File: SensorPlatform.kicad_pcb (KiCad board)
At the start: 2 copper layers, 70.5 x 88.9 mm, 37 parts, among them J1 Conn_01x19, J2 Conn_01x19, Q1 Q_NPN_BCE, Q2 Q_NPN_BCE, SW1 SW_Push, SW2 SW_Push, U1 AMS1117-3.3, U2 USB_CON8, U3 CP2102N, U4 ESP32-WROOM-32

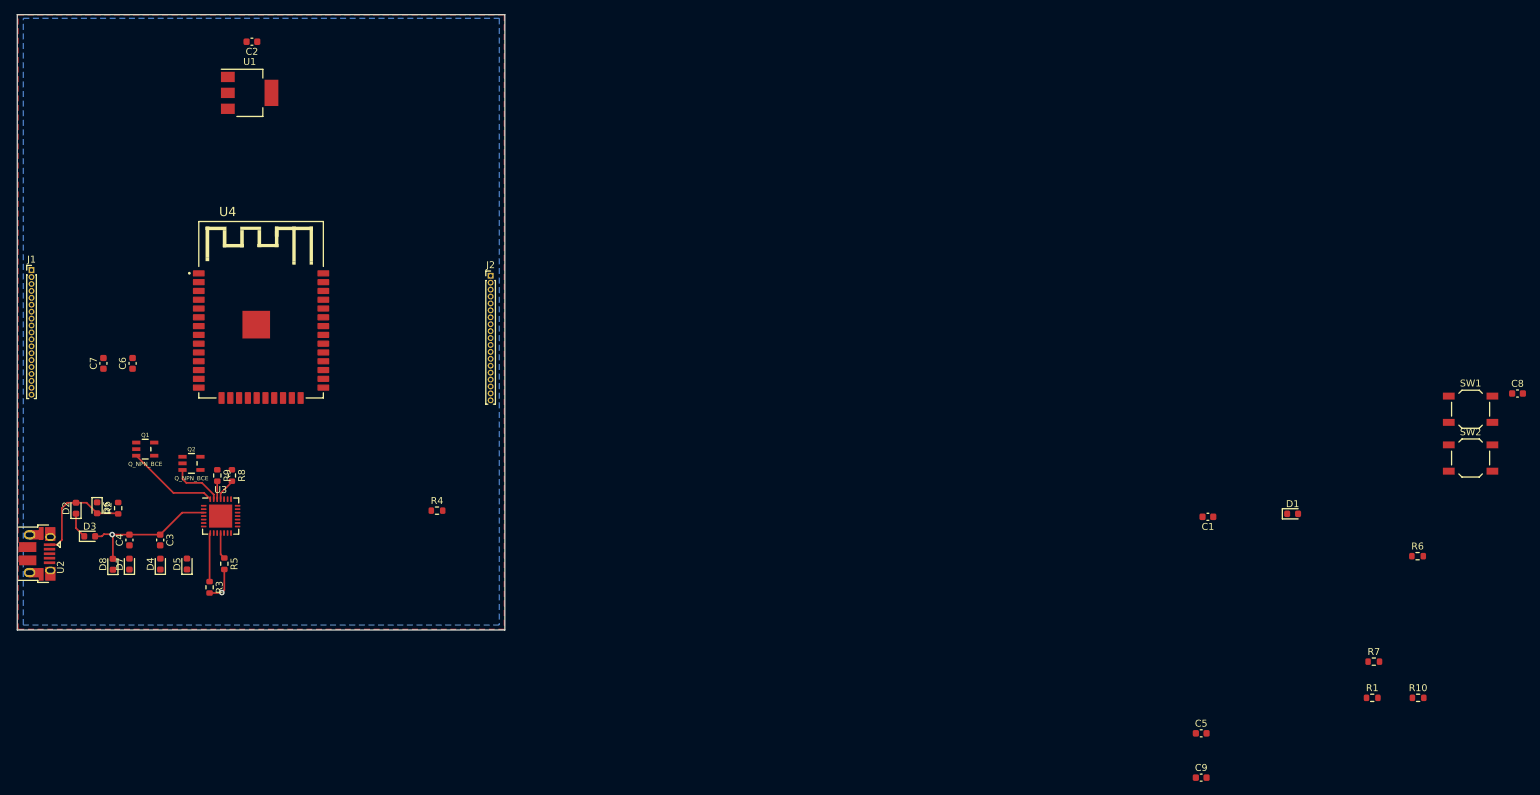
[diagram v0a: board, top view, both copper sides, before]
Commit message: Routed most PCB traces
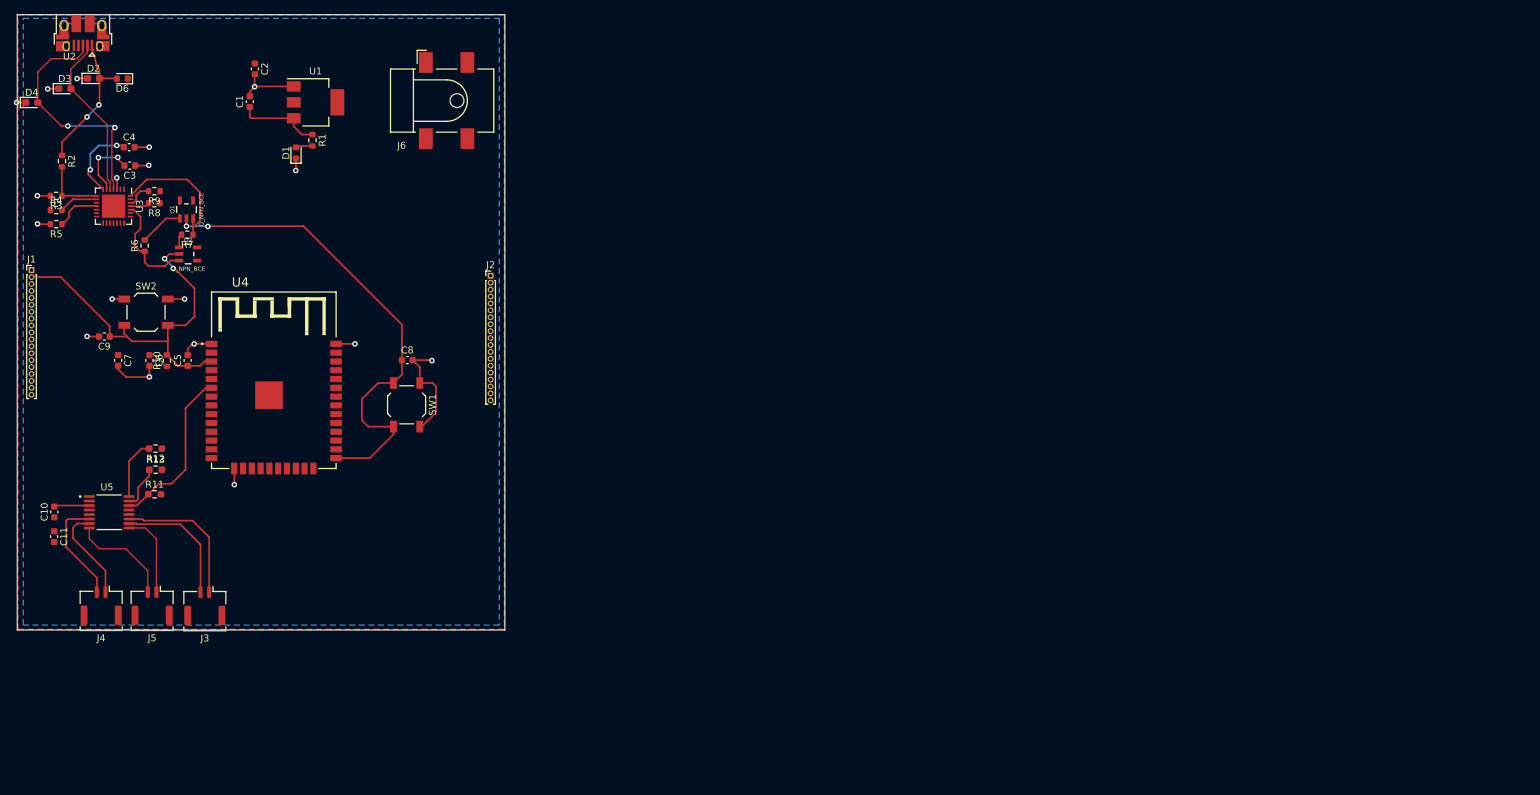
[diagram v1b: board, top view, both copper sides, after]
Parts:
- removed D5, D7, D8: D_Zener_Small_ALT, Diode_SMD:D_0603_1608Metric
- added C10: 0.1u, Capacitor_SMD:C_0603_1608Metric, F.Cu at (39.5, 108.5)
- added C11: 0.1u, Capacitor_SMD:C_0603_1608Metric, F.Cu at (39.5, 112.1)
- added J3: Conn_01x02, Connector_Molex:Molex_CLIK-Mate_502382-0270_1x02-1MP_P1.25mm_Vertical, F.Cu at (61.3, 122.0)
- added J4: Conn_01x02, Connector_Molex:Molex_CLIK-Mate_502382-0270_1x02-1MP_P1.25mm_Vertical, F.Cu at (46.3, 122.0)
- added J5: Conn_01x02, Connector_Molex:Molex_CLIK-Mate_502382-0270_1x02-1MP_P1.25mm_Vertical, F.Cu at (53.7, 122.0)
- added J6: Barrel_Jack, Connector_BarrelJack:BarrelJack_CLIFF_FC681465S_SMT_Horizontal, F.Cu at (96.2, 49.0)
- added R11: R, Resistor_SMD:R_0603_1608Metric_Pad0.98x0.95mm_HandSolder, F.Cu at (54.0, 105.9)
- added R12: R, Resistor_SMD:R_0603_1608Metric_Pad0.98x0.95mm_HandSolder, F.Cu at (54.2, 99.3)
- added R13: R, Resistor_SMD:R_0603_1608Metric_Pad0.98x0.95mm_HandSolder, F.Cu at (54.2, 102.4)
- added U5: ADS122C04IPWR, ADC:SOP65P640X120-16N, F.Cu at (47.5, 108.5)
- D2, D3, D4: value D_Zener_Small_ALT -> 1.5KExxCA; footprint Diode_SMD:D_0603_1608Metric -> Diode_SMD:D_0603_1608Metric_Pad1.05x0.95mm_HandSolder
- moved SW2 192.6 mm to (52.8, 79.6)
- moved R6 189.3 mm to (52.6, 70.0), turned to 90 degrees
- moved R10 187.3 mm to (55.8, 86.6), turned to 90 degrees
- moved R7 182.2 mm to (58.8, 68.4), turned to 180 degrees
- moved R1 173.1 mm to (76.8, 54.8), turned to -90 degrees
- moved C9 170.8 mm to (46.8, 83.1), turned to 180 degrees
- moved C8 160.5 mm to (90.5, 86.5)
- moved C5 156.1 mm to (58.8, 86.6), turned to 90 degrees
- moved SW1 153.8 mm to (90.5, 93.0), turned to -90 degrees
- moved D1 153.2 mm to (74.5, 56.6), turned to 90 degrees
- moved C1 150.9 mm to (67.8, 49.2), turned to 90 degrees
- moved U2 75.5 mm to (43.7, 39.3), turned to 180 degrees
- moved R4 70.1 mm to (39.8, 64.9)
- moved D4 69.2 mm to (36.3, 49.3), turned to 0 degrees
- moved D3 64.8 mm to (41.1, 47.3)
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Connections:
- D2 pad 1: Net-(D2-Pad1) -> GND
- D3 pad 1: Net-(D2-Pad1) -> GND
- D3 pad 2: GND -> USB_DN
- D4 pad 1: Net-(D4-Pad1) -> GND
- D4 pad 2: USB_DN -> USB_DP
- Q1 pad 2: /Micro USB 5v and USB-UART/IO0 -> IO0
- Q2 pad 2: /Micro USB 5v and USB-UART/EN -> EN
- Q2 pad 3: DSR -> RTS
- R6 pad 1: DSR -> RTS
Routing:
- net IO0: track 0.00 -> 71.5 mm, vias 0 -> 2
- net EN: track 0.00 -> 54.9 mm, vias 0 -> 2
- net GND: track 26.0 -> 71.0 mm, vias 2 -> 18
- net USB_DP: track 0.00 -> 35.0 mm, vias 0 -> 2
- net +3V3: track 0.00 -> 26.2 mm, vias 0 -> 4
- net IO34: track 0.00 -> 24.2 mm
- net USB_DN: track 0.00 -> 24.1 mm
- net AIN0: track 0.00 -> 20.6 mm
- net AIN1: track 0.00 -> 18.5 mm
- net AIN3: track 0.00 -> 15.6 mm
- net RTS: track 0.00 -> 15.3 mm
- net REFN: track 0.00 -> 15.0 mm
- net AIN2: track 0.00 -> 13.8 mm
- net REFP: track 0.00 -> 12.3 mm
- net Net-(C1-Pad1): track 0.00 -> 12.2 mm
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
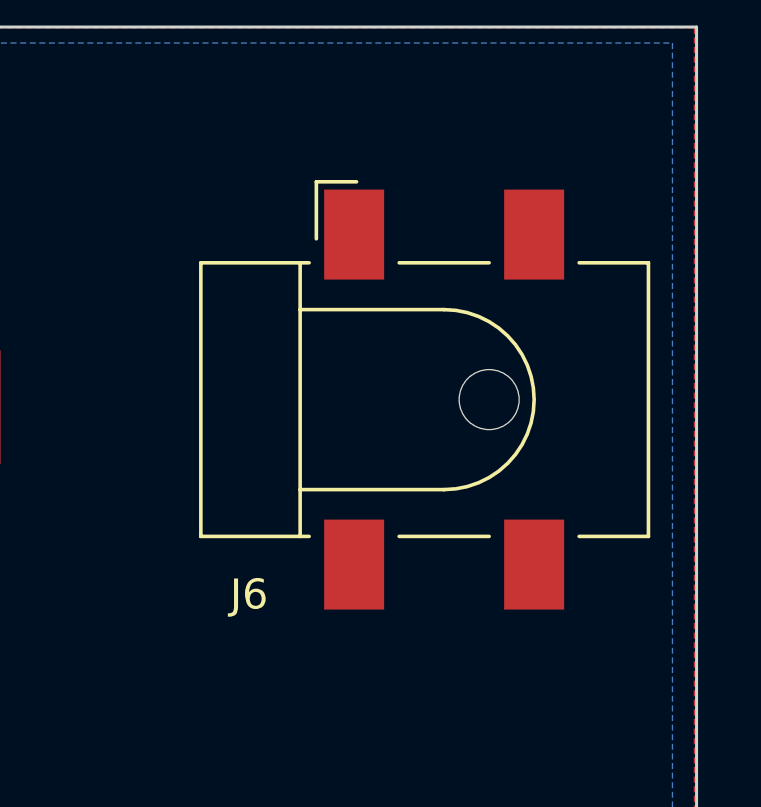
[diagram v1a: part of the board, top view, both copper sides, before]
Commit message: Added VOC and Optical Sensors
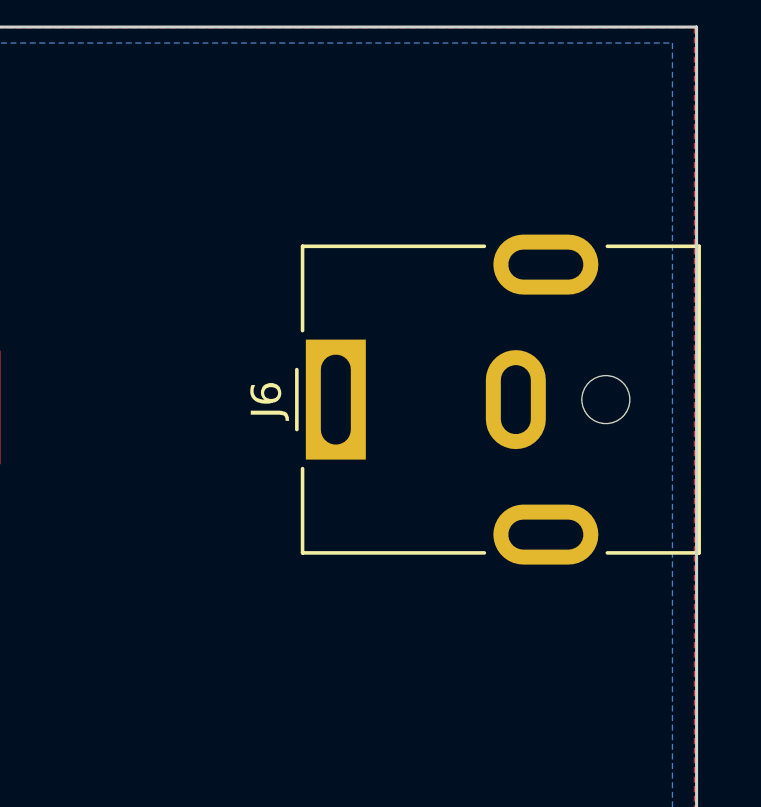
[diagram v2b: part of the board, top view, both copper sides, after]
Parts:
- J6: footprint Connector_BarrelJack:BarrelJack_CLIFF_FC681465S_SMT_Horizontal -> Connector_BarrelJack:BarrelJack_CUI_PJ-063AH_Horizontal
- moved J6 3.61 mm to (92.6, 49.0), turned to 90 degrees
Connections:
- C1 pad 1: Net-(C1-Pad1) -> +5V
- R1 pad 1: Net-(C1-Pad1) -> +5V
- U1 pad 3: Net-(C1-Pad1) -> +5V
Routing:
- net Net-(C1-Pad1): track 12.2 -> 0.00 mm
- net +5V: track 0.00 -> 12.2 mm

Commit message: Vertical Horizontal Traces
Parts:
- removed the C1 at (67.8, 49.2)
- removed the C10 at (39.5, 108.5)
- removed the C11 at (39.5, 112.1)
- removed the C2 at (68.5, 44.5)
- removed the C3 at (50.5, 58.4)
- removed the C4 at (50.4, 55.8)
- removed the C5 at (58.8, 86.6)
- removed the C6 at (53.3, 86.6)
- removed the C7 at (48.8, 86.6)
- removed the C8 at (90.5, 86.5)
- removed the C9 at (46.8, 83.1)
- removed the D1 at (74.5, 56.6)
- removed the D2 at (45.2, 45.8)
- removed the D3 at (41.1, 47.3)
- removed the D4 at (36.3, 49.3)
- removed the D6 at (49.4, 45.9)
- removed the J1 at (36.2, 73.5)
- removed the J2 at (102.6, 74.4)
- removed the J3 at (61.3, 122.0)
- removed the J4 at (46.3, 122.0)
- removed the J5 at (53.7, 122.0)
- removed the J6 at (92.6, 49.0)
- removed the Q1 at (58.6, 64.8)
- removed the Q2 at (58.9, 71.2)
- removed the R1 at (76.8, 54.8)
- removed the R10 at (55.8, 86.6)
- removed the R11 at (54.0, 105.9)
- removed the R12 at (54.2, 99.3)
- removed the R13 at (54.2, 102.4)
- removed the R2 at (40.6, 57.8)
- removed the R3 at (39.8, 62.8)
- removed the R4 at (39.8, 64.9)
- removed the R5 at (39.8, 66.9)
- removed the R6 at (52.6, 70.0)
- removed the R7 at (58.8, 68.4)
- removed the R8 at (54.0, 63.9)
- removed the R9 at (54.0, 62.1)
- removed the SW1 at (90.5, 93.0)
- removed the SW2 at (52.8, 79.6)
- removed the U1 at (77.3, 49.3)
- removed U2: USB_CON8, Connector_USB:USB_Micro-B_Amphenol_10103594-0001LF_Horizontal
- removed the U3 at (48.1, 64.3)
- removed the U4 at (71.3, 92.5)
- removed the U5 at (47.5, 108.5)
- added C1: 22u, Capacitor_SMD:C_0603_1608Metric, F.Cu at (452.6, 116.3)
- added C1: 22u, Capacitor_SMD:C_0603_1608Metric, F.Cu at (157.5, 110.2)
- added C10: 0.1u, Capacitor_SMD:C_0603_1608Metric, F.Cu at (411.8, 137.8)
- added C10: 0.1u, Capacitor_SMD:C_0603_1608Metric, F.Cu at (116.8, 131.7)
- added C11: 0.1u, Capacitor_SMD:C_0603_1608Metric, F.Cu at (109.7, 139.4)
- added C11: 0.1u, Capacitor_SMD:C_0603_1608Metric, F.Cu at (404.7, 145.4)
- added C12: 0.1u, Capacitor_SMD:C_0603_1608Metric, F.Cu at (422.2, 119.4)
- added C12: 0.1u, Capacitor_SMD:C_0603_1608Metric, F.Cu at (127.2, 113.3)
- added C13: 10u, Capacitor_SMD:C_0603_1608Metric, F.Cu at (116.7, 125.0)
- added C13: 10u, Capacitor_SMD:C_0603_1608Metric, F.Cu at (411.7, 131.1)
- added C14: 0.1u, Capacitor_SMD:C_0603_1608Metric, F.Cu at (411.9, 134.2)
- added C14: 0.1u, Capacitor_SMD:C_0603_1608Metric, F.Cu at (116.9, 128.1)
- added C15: 10u, Capacitor_SMD:C_0603_1608Metric, F.Cu at (412.5, 99.4)
- added C15: 10u, Capacitor_SMD:C_0603_1608Metric, F.Cu at (117.5, 93.3)
- added C16: 10u, Capacitor_SMD:C_0603_1608Metric, F.Cu at (416.8, 117.5)
- added C16: 10u, Capacitor_SMD:C_0603_1608Metric, F.Cu at (121.8, 111.4)
- added C17: 0.1u, Capacitor_SMD:C_0603_1608Metric, F.Cu at (118.0, 109.7)
- added C17: 0.1u, Capacitor_SMD:C_0603_1608Metric, F.Cu at (413.0, 115.8)
- added C18: 1u, Capacitor_SMD:C_0603_1608Metric, F.Cu at (139.4, 103.6)
- added C18: 1u, Capacitor_SMD:C_0603_1608Metric, F.Cu at (434.4, 109.7)
- added C19: 0.1u, Capacitor_SMD:C_0603_1608Metric, F.Cu at (99.9, 146.6)
- added C19: 0.1u, Capacitor_SMD:C_0603_1608Metric, F.Cu at (395.0, 153.0)
- added C2: 22u, Capacitor_SMD:C_0603_1608Metric, F.Cu at (157.5, 113.5)
- added C2: 22u, Capacitor_SMD:C_0603_1608Metric, F.Cu at (452.6, 119.6)
- added C20: 0.1u, Capacitor_SMD:C_0603_1608Metric, F.Cu at (399.1, 157.7)
- added C20: 0.1u, Capacitor_SMD:C_0603_1608Metric, F.Cu at (104.1, 151.6)
- added C21: 0.1u, Capacitor_SMD:C_0603_1608Metric, F.Cu at (87.6, 133.5)
- added C21: 0.1u, Capacitor_SMD:C_0603_1608Metric, F.Cu at (382.6, 139.6)
- added C22: 0.1u, Capacitor_SMD:C_0603_1608Metric, F.Cu at (395.2, 147.2)
- added C22: 0.1u, Capacitor_SMD:C_0603_1608Metric, F.Cu at (100.2, 141.1)
- added C3: 4.7u, Capacitor_SMD:C_0603_1608Metric, F.Cu at (155.8, 131.8)
- added C3: 4.7u, Capacitor_SMD:C_0603_1608Metric, F.Cu at (450.8, 137.9)
- added C4: 0.1u, Capacitor_SMD:C_0603_1608Metric, F.Cu at (174.6, 133.1)
- added C4: 0.1u, Capacitor_SMD:C_0603_1608Metric, F.Cu at (469.6, 139.2)
- added C5: 0.1u, Capacitor_SMD:C_0603_1608Metric, F.Cu at (114.6, 38.6)
- added C5: 0.1u, Capacitor_SMD:C_0603_1608Metric, F.Cu at (409.6, 44.7)
- added C6: 22u, Capacitor_SMD:C_0603_1608Metric, F.Cu at (403.3, 48.5)
- added C6: 22u, Capacitor_SMD:C_0603_1608Metric, F.Cu at (108.3, 42.4)
- added C7: 0.1u, Capacitor_SMD:C_0603_1608Metric, F.Cu at (108.3, 38.6)
- added C7: 0.1u, Capacitor_SMD:C_0603_1608Metric, F.Cu at (403.3, 44.7)
- added C8: 0.1u, Capacitor_SMD:C_0603_1608Metric, F.Cu at (147.1, 53.1)
- added C8: 0.1u, Capacitor_SMD:C_0603_1608Metric, F.Cu at (442.1, 59.2)
- added C9: 0.1u, Capacitor_SMD:C_0603_1608Metric, F.Cu at (409.6, 48.5)
- added C9: 0.1u, Capacitor_SMD:C_0603_1608Metric, F.Cu at (114.6, 42.4)
- added D1: LED, LED_SMD:LED_0603_1608Metric, F.Cu at (452.6, 122.7)
- added D1: LED, LED_SMD:LED_0603_1608Metric, F.Cu at (157.5, 116.6)
- added D10: D_TVS, Diode_SMD:D_0402_1005Metric_Pad0.77x0.64mm_HandSolder, F.Cu at (174.6, 127.8)
- added D10: D_TVS, Diode_SMD:D_0402_1005Metric_Pad0.77x0.64mm_HandSolder, F.Cu at (469.6, 133.8)
- added D11: D_TVS, Diode_SMD:D_0402_1005Metric_Pad0.77x0.64mm_HandSolder, F.Cu at (112.7, 110.4)
- added D11: D_TVS, Diode_SMD:D_0402_1005Metric_Pad0.77x0.64mm_HandSolder, F.Cu at (407.7, 116.5)
- added D12: D_TVS, Diode_SMD:D_0402_1005Metric_Pad0.77x0.64mm_HandSolder, F.Cu at (121.5, 120.9)
- added D12: D_TVS, Diode_SMD:D_0402_1005Metric_Pad0.77x0.64mm_HandSolder, F.Cu at (416.5, 127.0)
- added D13: D_Zener_Small_ALT, Diode_SMD:D_0603_1608Metric, F.Cu at (159.1, 104.9)
- added D13: D_Zener_Small_ALT, Diode_SMD:D_0603_1608Metric, F.Cu at (454.1, 111.0)
- added D2: 1.5KExxCA, Diode_SMD:D_0603_1608Metric_Pad1.05x0.95mm_HandSolder, F.Cu at (463.0, 144.8)
- added D2: 1.5KExxCA, Diode_SMD:D_0603_1608Metric_Pad1.05x0.95mm_HandSolder, F.Cu at (168.0, 138.7)
- added D3: 1.5KExxCA, Diode_SMD:D_0603_1608Metric_Pad1.05x0.95mm_HandSolder, F.Cu at (459.7, 149.2)
- added D3: 1.5KExxCA, Diode_SMD:D_0603_1608Metric_Pad1.05x0.95mm_HandSolder, F.Cu at (164.7, 143.1)
- added D4: 1.5KExxCA, Diode_SMD:D_0603_1608Metric_Pad1.05x0.95mm_HandSolder, F.Cu at (163.9, 138.7)
- added D4: 1.5KExxCA, Diode_SMD:D_0603_1608Metric_Pad1.05x0.95mm_HandSolder, F.Cu at (458.9, 144.8)
- added D5: LED, LED_SMD:LED_0603_1608Metric_Pad1.05x0.95mm_HandSolder, F.Cu at (109.3, 112.4)
- added D5: LED, LED_SMD:LED_0603_1608Metric_Pad1.05x0.95mm_HandSolder, F.Cu at (404.3, 118.5)
- added D6: D_Zener_Small_ALT, Diode_SMD:D_0603_1608Metric, F.Cu at (453.3, 155.7)
- added D6: D_Zener_Small_ALT, Diode_SMD:D_0603_1608Metric, F.Cu at (158.3, 149.6)
- added D7: LED, LED_SMD:LED_0603_1608Metric_Pad1.05x0.95mm_HandSolder, F.Cu at (110.9, 90.4)
- added D7: LED, LED_SMD:LED_0603_1608Metric_Pad1.05x0.95mm_HandSolder, F.Cu at (405.9, 96.5)
- added D8: LED, LED_SMD:LED_0603_1608Metric_Pad1.05x0.95mm_HandSolder, F.Cu at (416.5, 102.7)
- added D8: LED, LED_SMD:LED_0603_1608Metric_Pad1.05x0.95mm_HandSolder, F.Cu at (121.5, 97.6)
- added D9: LED, LED_SMD:LED_0603_1608Metric_Pad1.05x0.95mm_HandSolder, F.Cu at (126.2, 118.0)
- added D9: LED, LED_SMD:LED_0603_1608Metric_Pad1.05x0.95mm_HandSolder, F.Cu at (421.2, 124.1)
- added J1: Conn_01x19, Connector_PinHeader_2.54mm:PinHeader_1x19_P2.54mm_Vertical, F.Cu at (93.2, 47.5)
- added J1: Conn_01x19, Connector_PinHeader_2.54mm:PinHeader_1x19_P2.54mm_Vertical, F.Cu at (388.2, 53.6)
- added J10: 110990030, Seeed:SEEED_110990030, F.Cu at (162.5, 56.0)
- added J10: 110990030, Seeed:SEEED_110990030, F.Cu at (457.5, 62.1)
- added J2: Conn_01x19, Connector_PinHeader_2.54mm:PinHeader_1x19_P2.54mm_Vertical, F.Cu at (464.7, 53.6)
- added J2: Conn_01x19, Connector_PinHeader_2.54mm:PinHeader_1x19_P2.54mm_Vertical, F.Cu at (169.7, 47.5)
- added J3: Conn_01x02, Connector_PinHeader_2.54mm:PinHeader_1x02_P2.54mm_Vertical, F.Cu at (105.8, 142.7)
- added J3: Conn_01x02, Connector_PinHeader_2.54mm:PinHeader_1x02_P2.54mm_Vertical, F.Cu at (400.8, 148.8)
- added J4: Conn_01x02, Connector_PinHeader_2.54mm:PinHeader_1x02_P2.54mm_Vertical, F.Cu at (110.9, 142.9)
- added J4: Conn_01x02, Connector_PinHeader_2.54mm:PinHeader_1x02_P2.54mm_Vertical, F.Cu at (405.9, 149.0)
- added J5: Conn_01x02, Connector_PinHeader_2.54mm:PinHeader_1x02_P2.54mm_Vertical, F.Cu at (413.6, 148.4)
- added J5: Conn_01x02, Connector_PinHeader_2.54mm:PinHeader_1x02_P2.54mm_Vertical, F.Cu at (118.6, 142.3)
- added J6: Barrel_Jack, Connector_BarrelJack:BarrelJack_CUI_PJ-063AH_Horizontal, F.Cu at (459.3, 110.7)
- added J6: Barrel_Jack, Connector_BarrelJack:BarrelJack_CUI_PJ-063AH_Horizontal, F.Cu at (164.2, 104.6)
- added J7: Conn_01x04, Connector_PinHeader_2.54mm:PinHeader_1x04_P2.54mm_Vertical, F.Cu at (110.0, 54.9)
- added J7: Conn_01x04, Connector_PinHeader_2.54mm:PinHeader_1x04_P2.54mm_Vertical, F.Cu at (405.1, 61.0)
- added J8: Conn_01x08, Connector_PinHeader_2.54mm:PinHeader_1x08_P2.54mm_Vertical, F.Cu at (93.2, 100.0)
- added J8: Conn_01x08, Connector_PinHeader_2.54mm:PinHeader_1x08_P2.54mm_Vertical, F.Cu at (388.2, 106.1)
- added J9: QWIIC_CONNECTORSR, SparkfunConnectors:1X04_1MM_RA_STRESSRELIEF, F.Cu at (157.3, 67.6)
- added J9: QWIIC_CONNECTORSR, SparkfunConnectors:1X04_1MM_RA_STRESSRELIEF, F.Cu at (452.3, 73.6)
- added JP1: Jumper, Jumper:SolderJumper-2_P1.3mm_Bridged_RoundedPad1.0x1.5mm, F.Cu at (97.4, 118.3)
- added JP1: Jumper, Jumper:SolderJumper-2_P1.3mm_Bridged_RoundedPad1.0x1.5mm, F.Cu at (392.4, 124.4)
- added Q1: Q_NPN_BCE, Package_TO_SOT_SMD:SOT-23, F.Cu at (443.2, 141.2)
- added Q1: Q_NPN_BCE, Package_TO_SOT_SMD:SOT-23, F.Cu at (148.2, 135.1)
- added Q2: Q_NPN_BCE, Package_TO_SOT_SMD:SOT-23, F.Cu at (454.6, 134.3)
- added Q2: Q_NPN_BCE, Package_TO_SOT_SMD:SOT-23, F.Cu at (159.6, 128.3)
- added R1: 2k, Resistor_SMD:R_0603_1608Metric_Pad0.98x0.95mm_HandSolder, F.Cu at (153.5, 116.6)
- added R1: 2k, Resistor_SMD:R_0603_1608Metric_Pad0.98x0.95mm_HandSolder, F.Cu at (448.5, 122.7)
- added R10: 10k, Resistor_SMD:R_0603_1608Metric_Pad0.98x0.95mm_HandSolder, F.Cu at (395.9, 44.7)
- added R10: 10k, Resistor_SMD:R_0603_1608Metric_Pad0.98x0.95mm_HandSolder, F.Cu at (100.9, 38.6)
- added R11: R, Resistor_SMD:R_0603_1608Metric_Pad0.98x0.95mm_HandSolder, F.Cu at (395.3, 144.2)
- added R11: R, Resistor_SMD:R_0603_1608Metric_Pad0.98x0.95mm_HandSolder, F.Cu at (100.4, 139.4)
- added R12: R, Resistor_SMD:R_0603_1608Metric_Pad0.98x0.95mm_HandSolder, F.Cu at (90.5, 135.1)
- added R12: R, Resistor_SMD:R_0603_1608Metric_Pad0.98x0.95mm_HandSolder, F.Cu at (385.5, 141.2)
- added R13: R, Resistor_SMD:R_0603_1608Metric_Pad0.98x0.95mm_HandSolder, F.Cu at (395.1, 140.8)
- added R13: R, Resistor_SMD:R_0603_1608Metric_Pad0.98x0.95mm_HandSolder, F.Cu at (100.0, 134.7)
- added R14: R, Resistor_SMD:R_0603_1608Metric_Pad0.98x0.95mm_HandSolder, F.Cu at (389.2, 137.8)
- added R14: R, Resistor_SMD:R_0603_1608Metric_Pad0.98x0.95mm_HandSolder, F.Cu at (93.6, 131.8)
- added R15: R, Resistor_SMD:R_0603_1608Metric_Pad0.98x0.95mm_HandSolder, F.Cu at (385.9, 137.8)
- added R15: R, Resistor_SMD:R_0603_1608Metric_Pad0.98x0.95mm_HandSolder, F.Cu at (90.0, 131.8)
- added R16: 10k, Resistor_SMD:R_0603_1608Metric_Pad0.98x0.95mm_HandSolder, F.Cu at (105.3, 107.7)
- added R16: 10k, Resistor_SMD:R_0603_1608Metric_Pad0.98x0.95mm_HandSolder, F.Cu at (400.3, 113.8)
- added R17: 2.2k, Resistor_SMD:R_0603_1608Metric_Pad0.98x0.95mm_HandSolder, F.Cu at (121.4, 100.8)
- added R17: 2.2k, Resistor_SMD:R_0603_1608Metric_Pad0.98x0.95mm_HandSolder, F.Cu at (416.4, 106.9)
- added R18: 10k, Resistor_SMD:R_0603_1608Metric_Pad0.98x0.95mm_HandSolder, F.Cu at (99.5, 102.1)
- added R18: 10k, Resistor_SMD:R_0603_1608Metric_Pad0.98x0.95mm_HandSolder, F.Cu at (394.5, 108.2)
- added R19: 2.2k, Resistor_SMD:R_0603_1608Metric_Pad0.98x0.95mm_HandSolder, F.Cu at (120.2, 104.8)
- added R19: 2.2k, Resistor_SMD:R_0603_1608Metric_Pad0.98x0.95mm_HandSolder, F.Cu at (415.2, 110.9)
- added R2: 22.1k, Resistor_SMD:R_0603_1608Metric_Pad0.98x0.95mm_HandSolder, F.Cu at (453.3, 151.9)
- added R2: 22.1k, Resistor_SMD:R_0603_1608Metric_Pad0.98x0.95mm_HandSolder, F.Cu at (158.3, 145.8)
- added R20: 0, Resistor_SMD:R_0603_1608Metric_Pad0.98x0.95mm_HandSolder, F.Cu at (115.0, 100.9)
- added R20: 0, Resistor_SMD:R_0603_1608Metric_Pad0.98x0.95mm_HandSolder, F.Cu at (410.0, 107.0)
- added R21: 0, Resistor_SMD:R_0603_1608Metric_Pad0.98x0.95mm_HandSolder, F.Cu at (111.2, 103.6)
- added R21: 0, Resistor_SMD:R_0603_1608Metric_Pad0.98x0.95mm_HandSolder, F.Cu at (408.1, 110.1)
- added R22: 10k, Resistor_SMD:R_0603_1608Metric_Pad0.98x0.95mm_HandSolder, F.Cu at (396.2, 102.1)
- added R22: 10k, Resistor_SMD:R_0603_1608Metric_Pad0.98x0.95mm_HandSolder, F.Cu at (101.2, 96.1)
- added R23: 10k, Resistor_SMD:R_0603_1608Metric_Pad0.98x0.95mm_HandSolder, F.Cu at (106.6, 93.9)
- added R23: 10k, Resistor_SMD:R_0603_1608Metric_Pad0.98x0.95mm_HandSolder, F.Cu at (401.6, 100.0)
- added R24: 200, Resistor_SMD:R_0603_1608Metric_Pad0.98x0.95mm_HandSolder, F.Cu at (108.3, 108.2)
- added R24: 200, Resistor_SMD:R_0603_1608Metric_Pad0.98x0.95mm_HandSolder, F.Cu at (403.3, 114.3)
- added R25: 200, Resistor_SMD:R_0603_1608Metric_Pad0.98x0.95mm_HandSolder, F.Cu at (410.1, 102.6)
- added R25: 200, Resistor_SMD:R_0603_1608Metric_Pad0.98x0.95mm_HandSolder, F.Cu at (115.0, 97.6)
- added R26: R, Resistor_SMD:R_0603_1608Metric_Pad0.98x0.95mm_HandSolder, F.Cu at (126.1, 87.8)
- added R26: R, Resistor_SMD:R_0603_1608Metric_Pad0.98x0.95mm_HandSolder, F.Cu at (418.6, 93.9)
- added R27: 200, Resistor_SMD:R_0603_1608Metric_Pad0.98x0.95mm_HandSolder, F.Cu at (131.4, 118.1)
- added R27: 200, Resistor_SMD:R_0603_1608Metric_Pad0.98x0.95mm_HandSolder, F.Cu at (426.4, 124.2)
- added R28: R, Resistor_SMD:R_0603_1608Metric_Pad0.98x0.95mm_HandSolder, F.Cu at (98.2, 128.0)
- added R28: R, Resistor_SMD:R_0603_1608Metric_Pad0.98x0.95mm_HandSolder, F.Cu at (393.3, 134.1)
- added R29: R, Resistor_SMD:R_0603_1608Metric_Pad0.98x0.95mm_HandSolder, F.Cu at (403.1, 92.9)
- added R29: R, Resistor_SMD:R_0603_1608Metric_Pad0.98x0.95mm_HandSolder, F.Cu at (108.1, 86.9)
- added R3: 47.5k, Resistor_SMD:R_0603_1608Metric_Pad0.98x0.95mm_HandSolder, F.Cu at (453.3, 148.8)
- added R3: 47.5k, Resistor_SMD:R_0603_1608Metric_Pad0.98x0.95mm_HandSolder, F.Cu at (158.3, 142.7)
- added R30: R, Resistor_SMD:R_0603_1608Metric_Pad0.98x0.95mm_HandSolder, F.Cu at (405.2, 84.1)
- added R30: R, Resistor_SMD:R_0603_1608Metric_Pad0.98x0.95mm_HandSolder, F.Cu at (110.2, 78.0)
- added R31: R, Resistor_SMD:R_0603_1608Metric_Pad0.98x0.95mm_HandSolder, F.Cu at (100.1, 144.9)
- added R31: R, Resistor_SMD:R_0603_1608Metric_Pad0.98x0.95mm_HandSolder, F.Cu at (395.2, 151.3)
- added R32: R, Resistor_SMD:R_0603_1608Metric_Pad0.98x0.95mm_HandSolder, F.Cu at (107.2, 151.7)
- added R32: R, Resistor_SMD:R_0603_1608Metric_Pad0.98x0.95mm_HandSolder, F.Cu at (402.2, 157.7)
- added R33: R, Resistor_SMD:R_0603_1608Metric_Pad0.98x0.95mm_HandSolder, F.Cu at (405.7, 157.7)
- added R33: R, Resistor_SMD:R_0603_1608Metric_Pad0.98x0.95mm_HandSolder, F.Cu at (110.7, 151.6)
- added R34: 0, Resistor_SMD:R_0603_1608Metric_Pad0.98x0.95mm_HandSolder, F.Cu at (395.6, 123.5)
- added R34: 0, Resistor_SMD:R_0603_1608Metric_Pad0.98x0.95mm_HandSolder, F.Cu at (100.6, 117.4)
- added R35: 0, Resistor_SMD:R_0603_1608Metric_Pad0.98x0.95mm_HandSolder, F.Cu at (111.2, 93.9)
- added R35: 0, Resistor_SMD:R_0603_1608Metric_Pad0.98x0.95mm_HandSolder, F.Cu at (406.2, 100.0)
- added R36: R, Resistor_SMD:R_0603_1608Metric_Pad0.98x0.95mm_HandSolder, F.Cu at (100.0, 142.9)
- added R36: R, Resistor_SMD:R_0603_1608Metric_Pad0.98x0.95mm_HandSolder, F.Cu at (395.1, 149.0)
- added R4: 2k, Resistor_SMD:R_0603_1608Metric_Pad0.98x0.95mm_HandSolder, F.Cu at (464.8, 141.4)
- added R4: 2k, Resistor_SMD:R_0603_1608Metric_Pad0.98x0.95mm_HandSolder, F.Cu at (169.7, 135.3)
- added R5: 10k, Resistor_SMD:R_0603_1608Metric_Pad0.98x0.95mm_HandSolder, F.Cu at (174.6, 135.4)
- added R5: 10k, Resistor_SMD:R_0603_1608Metric_Pad0.98x0.95mm_HandSolder, F.Cu at (469.6, 141.5)
- added R6: 10k, Resistor_SMD:R_0603_1608Metric_Pad0.98x0.95mm_HandSolder, F.Cu at (159.8, 133.3)
- added R6: 10k, Resistor_SMD:R_0603_1608Metric_Pad0.98x0.95mm_HandSolder, F.Cu at (454.8, 139.4)
- added R7: 10k, Resistor_SMD:R_0603_1608Metric_Pad0.98x0.95mm_HandSolder, F.Cu at (154.5, 127.2)
- added R7: 10k, Resistor_SMD:R_0603_1608Metric_Pad0.98x0.95mm_HandSolder, F.Cu at (449.5, 133.3)
- added R8: 0, Resistor_SMD:R_0603_1608Metric_Pad0.98x0.95mm_HandSolder, F.Cu at (447.2, 130.0)
- added R8: 0, Resistor_SMD:R_0603_1608Metric_Pad0.98x0.95mm_HandSolder, F.Cu at (152.2, 123.9)
- added R9: 0, Resistor_SMD:R_0603_1608Metric_Pad0.98x0.95mm_HandSolder, F.Cu at (468.1, 129.0)
- added R9: 0, Resistor_SMD:R_0603_1608Metric_Pad0.98x0.95mm_HandSolder, F.Cu at (173.0, 122.9)
- added REF**: TestPoint_Pad_D2.5mm, TestPoint:TestPoint_Pad_D2.5mm, F.Cu at (142.8, 126.7)
- added REF**: TestPoint_Pad_D2.5mm, TestPoint:TestPoint_Pad_D2.5mm, F.Cu at (437.8, 132.8)
- added REF**: MountingHole_2.2mm_M2, MountingHole:MountingHole_2.2mm_M2, F.Cu at (467.1, 47.4)
- added REF**: MountingHole_2.2mm_M2, MountingHole:MountingHole_2.2mm_M2, F.Cu at (172.1, 149.5)
- added REF**: MountingHole_2.2mm_M2, MountingHole:MountingHole_2.2mm_M2, F.Cu at (172.1, 41.3)
- added REF**: MountingHole_2.2mm_M2, MountingHole:MountingHole_2.2mm_M2, F.Cu at (386.6, 155.6)
- added REF**: MountingHole_2.2mm_M2, MountingHole:MountingHole_2.2mm_M2, F.Cu at (91.6, 149.5)
- added REF**: MountingHole_2.2mm_M2, MountingHole:MountingHole_2.2mm_M2, F.Cu at (467.1, 155.6)
- added REF**: MountingHole_2.2mm_M2, MountingHole:MountingHole_2.2mm_M2, F.Cu at (91.6, 41.3)
- added REF**: MountingHole_2.2mm_M2, MountingHole:MountingHole_2.2mm_M2, F.Cu at (386.6, 47.4)
- added SW1: SW_Push, Button_Switch_SMD:SW_SPST_TL3342, F.Cu at (426.9, 69.3)
- added SW1: SW_Push, Button_Switch_SMD:SW_SPST_TL3342, F.Cu at (131.9, 63.2)
- added SW2: SW_Push, Button_Switch_SMD:SW_SPST_TL3342, F.Cu at (440.1, 69.3)
- added SW2: SW_Push, Button_Switch_SMD:SW_SPST_TL3342, F.Cu at (145.1, 63.2)
- added SW3: SW_Push, Button_Switch_SMD:SW_SPST_TL3342, F.Cu at (105.8, 126.1)
- added SW3: SW_Push, Button_Switch_SMD:SW_SPST_TL3342, F.Cu at (400.9, 132.2)
- added SW4: SW_Push, Button_Switch_SMD:SW_SPST_TL3342, F.Cu at (396.5, 91.9)
- added SW4: SW_Push, Button_Switch_SMD:SW_SPST_TL3342, F.Cu at (101.5, 85.9)
- added SW5: SW_Push, Button_Switch_SMD:SW_SPST_TL3342, F.Cu at (116.4, 85.9)
- added SW5: SW_Push, Button_Switch_SMD:SW_SPST_TL3342, F.Cu at (411.4, 92.0)
- added SW6: SW_Push, Button_Switch_SMD:SW_SPST_TL3342, F.Cu at (101.4, 75.9)
- added SW6: SW_Push, Button_Switch_SMD:SW_SPST_TL3342, F.Cu at (396.4, 82.0)
- added U1: AMS1117-3.3, Package_TO_SOT_SMD:SOT-223-3_TabPin2, F.Cu at (164.7, 119.0)
- added U1: AMS1117-3.3, Package_TO_SOT_SMD:SOT-223-3_TabPin2, F.Cu at (459.7, 125.1)
- added U10: AT25SF041, Package_SO:SO-8_3.9x4.9mm_P1.27mm, F.Cu at (132.5, 104.7)
- added U10: AT25SF041, Package_SO:SO-8_3.9x4.9mm_P1.27mm, F.Cu at (427.6, 110.8)
- added U3: CP2102N, Package_DFN_QFN:QFN-28-1EP_5x5mm_P0.5mm_EP3.35x3.35mm, F.Cu at (169.2, 130.2)
- added U3: CP2102N, Package_DFN_QFN:QFN-28-1EP_5x5mm_P0.5mm_EP3.35x3.35mm, F.Cu at (464.2, 136.3)
- added U4: ESP32-WROOM-32, ESP32-WROOM-32:MODULE_ESP-WROOM-32, F.Cu at (427.1, 50.7)
- added U4: ESP32-WROOM-32, ESP32-WROOM-32:MODULE_ESP-WROOM-32, F.Cu at (132.1, 44.7)
- added U5: ADS122C04IPWR, ADS122C04IPWR:SOP65P640X120-16N, F.Cu at (92.4, 139.0)
- added U5: ADS122C04IPWR, ADS122C04IPWR:SOP65P640X120-16N, F.Cu at (387.4, 145.1)
- added U6: ZMOD4410AI3V, ZMOD4410-LGA-12_3x3:ZMOD4410-LGA-12_3x3, F.Cu at (92.7, 128.0)
- added U6: ZMOD4410AI3V, ZMOD4410-LGA-12_3x3:ZMOD4410-LGA-12_3x3, F.Cu at (387.7, 134.1)
- added U7: AS72652, Package_LGA:AMS_LGA-20_4.7x4.5mm_P0.65mm, F.Cu at (104.8, 116.1)
- added U7: AS72652, Package_LGA:AMS_LGA-20_4.7x4.5mm_P0.65mm, F.Cu at (399.8, 122.2)
- added U8: AS72651, Package_LGA:AMS_LGA-20_4.7x4.5mm_P0.65mm, F.Cu at (402.0, 106.5)
- added U8: AS72651, Package_LGA:AMS_LGA-20_4.7x4.5mm_P0.65mm, F.Cu at (107.0, 100.6)
- added U9: AS72653, Package_LGA:AMS_LGA-20_4.7x4.5mm_P0.65mm, F.Cu at (117.3, 116.1)
- added U9: AS72653, Package_LGA:AMS_LGA-20_4.7x4.5mm_P0.65mm, F.Cu at (412.3, 122.2)
- added locked: USB_CON8, Connector_USB:USB_Micro-B_Amphenol_10103594-0001LF_Horizontal, F.Cu at (468.5, 146.9)
- added locked: USB_CON8, Connector_USB:USB_Micro-B_Amphenol_10103594-0001LF_Horizontal, F.Cu at (173.5, 140.8)
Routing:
- net +5V: track 12.2 -> 256.8 mm, vias 0 -> 12
- net +3V3: track 26.2 -> 201.7 mm, vias 4 -> 84
- net GND: track 71.0 -> 236.6 mm, vias 18 -> 75
- net OpticalSensorInterrupt: track 0.00 -> 92.5 mm, vias 0 -> 6
- net SLV2ResetPin: track 0.00 -> 92.3 mm, vias 0 -> 5
- net AS72652AndAS72653_SCL: track 0.00 -> 80.6 mm, vias 0 -> 6
- net OpticalSPIMISO: track 0.00 -> 78.6 mm, vias 0 -> 7
- net IO0: track 71.5 -> 5.37 mm, vias 2 -> 0
- net OpticalSensorResetPin: track 0.00 -> 65.4 mm, vias 0 -> 2
- net AS72652AndAS72653_SDA: track 0.00 -> 49.4 mm, vias 0 -> 8
- net ~{CS}: track 0.00 -> 43.7 mm, vias 0 -> 5
- net SDA: track 0.00 -> 42.5 mm, vias 0 -> 2
- net Net-(C21-Pad2): track 0.00 -> 40.4 mm
- net SENSOR_VN: track 0.00 -> 35.5 mm
- net SLV2Reset: track 0.00 -> 35.1 mm, vias 0 -> 2
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- added copper zone on In2.Cu, net +3V3
- added copper zone on In1.Cu, net GND
- removed copper zone on F.Cu, net +3V3
- removed copper zone on B.Cu, net GND
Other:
- board size 70.5 x 88.9 mm -> 386.7 x 125.6 mm
- copper layers 2 -> 4
